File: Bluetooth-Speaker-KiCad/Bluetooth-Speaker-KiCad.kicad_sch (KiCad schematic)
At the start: 34 parts, among them J1 USB4105-GF-A, J2 Screw_Terminal_01x02, J3 Screw_Terminal_01x02, Q1 Q_PMOS_DSG, SW1 SW_Push, SW2 SW_Push, U1 TPD4E02B04DQA, U2 MAX1811, U3 RT6150B-33GQW, U4 MAX98357A, U5 ESP32-C3-WROOM-02

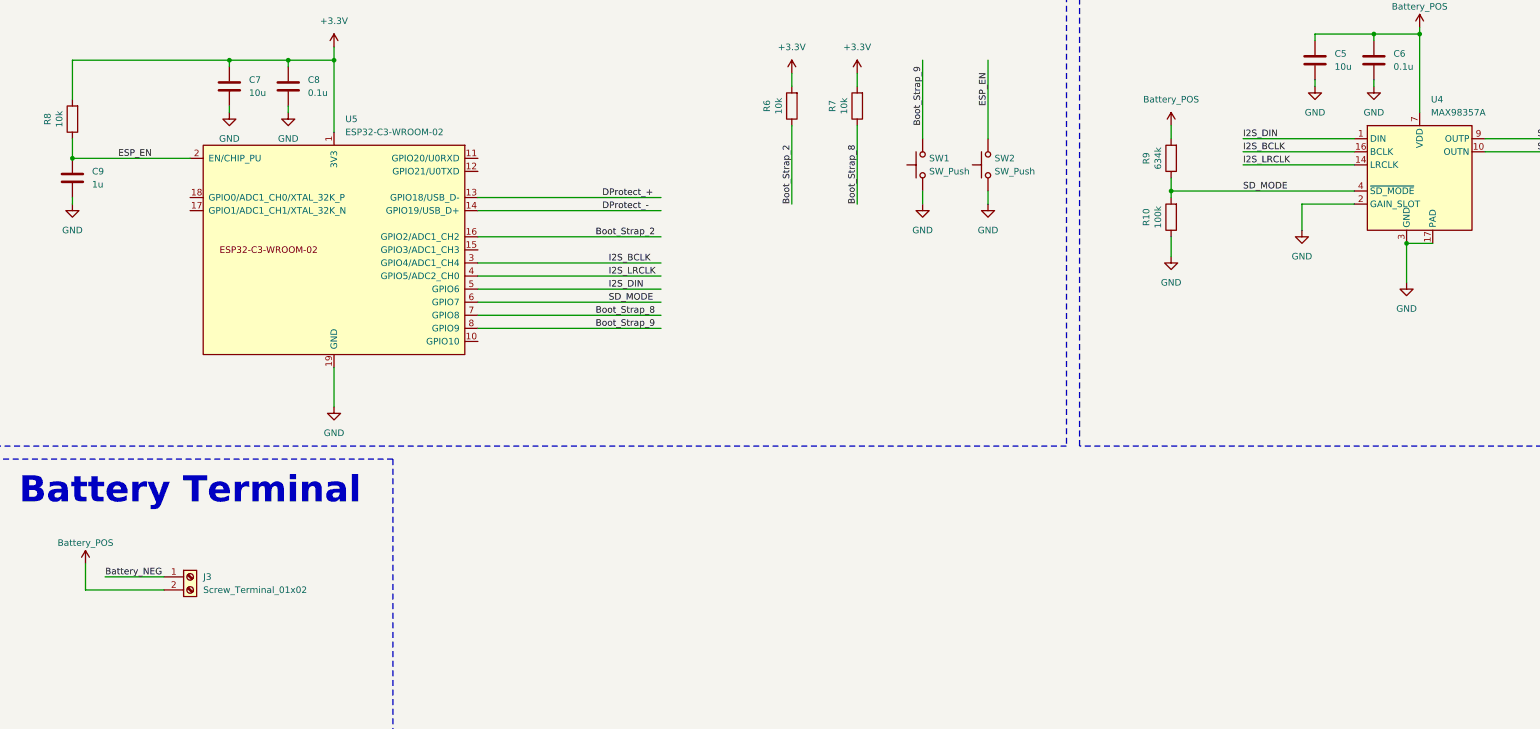
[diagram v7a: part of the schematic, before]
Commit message: Updated layout
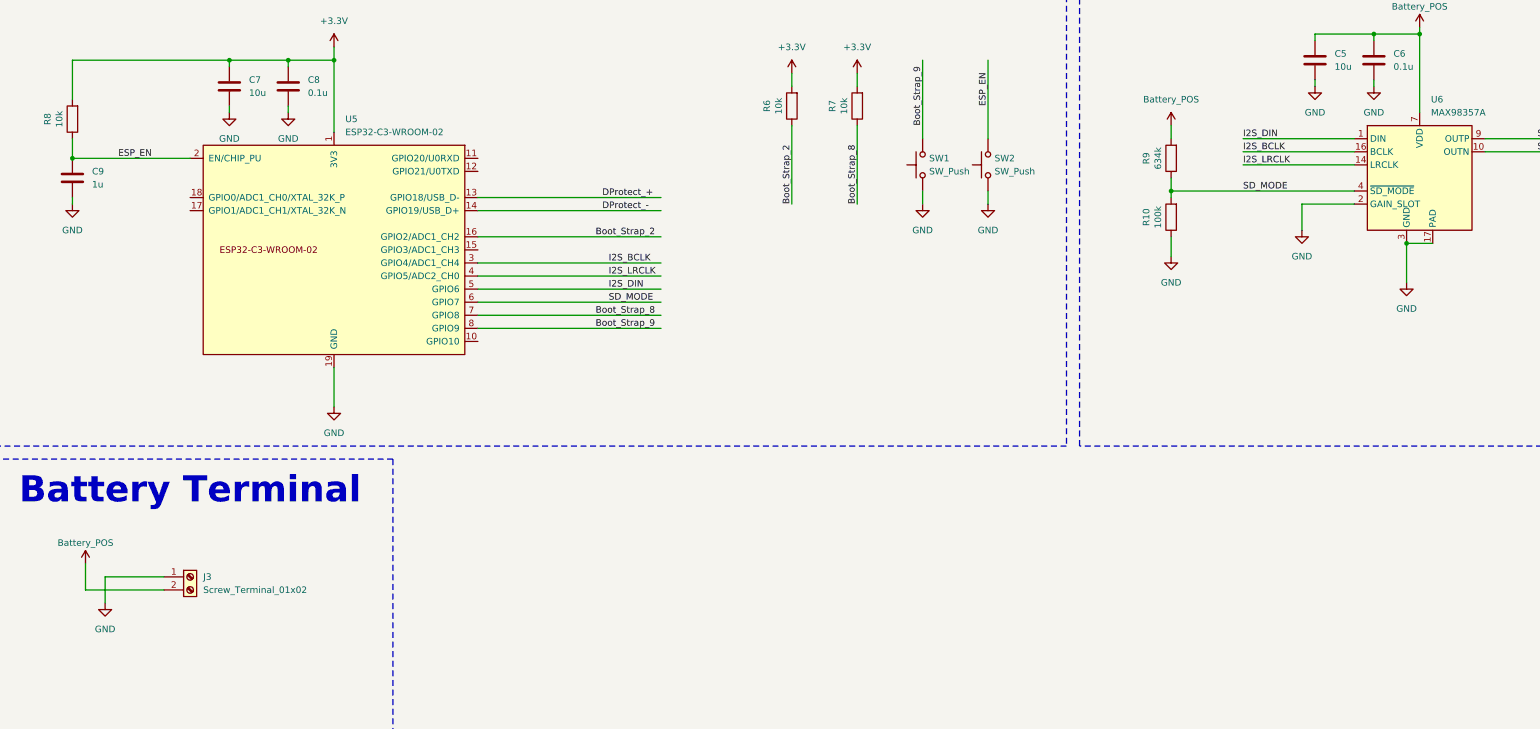
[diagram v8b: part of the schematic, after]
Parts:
- removed U4: MAX98357A, Package_DFN_QFN:TQFN-16-1EP_3x3mm_P0.5mm_EP1.23x1.23mm, symbol Audio:MAX98357A
- added U6: MAX98357A, Package_DFN_QFN:TQFN-16-1EP_3x3mm_P0.5mm_EP1.23x1.23mm_ThermalVias, symbol Audio:MAX98357A
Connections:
- net Battery_NEG is gone; now on net GND: J3.1 (Pin_1)
- net Battery_POS: now also U6.7 (VDD), U6.8 (VDD)
- net GND: now also U6.11 (GND), U6.15 (GND), U6.17 (PAD), U6.2 (GAIN_SLOT), U6.3 (GND)
- net I2S_BCLK: now also U6.16 (BCLK)
- net I2S_DIN: now also U6.1 (DIN)
- net I2S_LRCLK: now also U6.14 (LRCLK)
- net SD_MODE: now also U6.4 (~{SD_MODE})
- net Speaker_NEG: now also U6.10 (OUTN)
- net Speaker_POS: now also U6.9 (OUTP)
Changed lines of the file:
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@@
 	)
 	(junction
-		(at 298.45 177.8)
-		(diameter 0)
-		(color 0 0 0 0)
-	)
-	(junction
 		(at 186.69 63.5)
 		(diameter 0)
@@
 	)
 	(junction
+		(at 298.45 177.8)
+		(diameter 0)
+		(color 0 0 0 0)
+	)
+	(junction
 		(at 237.49 60.96)
 		(diameter 0)
@@
 	(wire
 		(pts
+			(xy 45.72 242.57) (xy 45.72 247.65)
+		)
+		(stroke
+			(width 0)
+			(type default)
+		)
+	)
+	(wire
+		(pts
 			(xy 252.73 167.64) (xy 252.73 168.91)
 		)
@@
 		)
 	)
-	(label "Battery_NEG"
-		(at 45.72 242.57 0)
-		(fields_autoplaced yes)
-		(effects
-			(font
-				(size 1.27 1.27)
-			)
-			(justify left bottom)
-		)
-	)
 	(symbol
 		(lib_id "power:+3.3V")
@@
 	)
 	(symbol
+		(lib_id "Audio:MAX98357A")
+		(at 300.99 165.1 0)
+		(unit 1)
+		(exclude_from_sim no)
+		(in_bom yes)
+		(on_board yes)
+		(dnp no)
+		(fields_autoplaced yes)
+		(property "Reference" "U6"
+			(at 303.1841 149.86 0)
+			(effects
+				(font
+					(size 1.27 1.27)
+				)
+				(justify left)
+			)
+		)
+		(property "Value" "MAX98357A"
+			(at 303.1841 152.4 0)
+			(effects
+				(font
+					(size 1.27 1.27)
+				)
+				(justify left)
+			)
+		)
+		(property "Footprint" "Package_DFN_QFN:TQFN-16-1EP_3x3mm_P0.5mm_EP1.23x1.23mm_ThermalVias"
+			(at 299.72 167.64 0)
+			(effects
+				(font
+					(size 1.27 1.27)
+				)
+				(hide yes)
+			)
+		)
+		(property "Datasheet" "https://www.analog.com/media/en/technical-documentation/data-sheets/MAX98357A-MAX98357B.pdf"
+			(at 300.99 167.64 0)
+			(effects
+				(font
+					(size 1.27 1.27)
+				)
+				(hide yes)
+			)
+		)
+		(property "Description" "Mono DAC with amplifier, I2S, PCM, TDM, 32-bit, 96khz, 3.2W, TQFP-16"
+			(at 300.99 165.1 0)
+			(effects
+				(font
+					(size 1.27 1.27)
+				)
+				(hide yes)
+			)
+		)
+		(pin "3"
+		)
+		(pin "4"
+		)
+		(pin "6"
+		)
+		(pin "5"
+		)
+		(pin "10"
+		)
+		(pin "17"
+		)
+		(pin "8"
+		)
+		(pin "13"
+		)
+		(pin "12"
+		)
+		(pin "1"
+		)
+		(pin "16"
+		)
+		(pin "15"
+		)
+		(pin "14"
+		)
+		(pin "2"
+		)
+		(pin "11"
+		)
+		(pin "7"
+		)
+		(pin "9"
+		)
+		(instances
+			(project ""
+				(path "/d4a3b0fc-2821-415b-ab7a-919b4d2a2ab9"
+					(reference "U6")
+					(unit 1)
+				)
+			)
+		)
+	)
+	(symbol
 		(lib_id "power:GND")
 		(at 278.13 175.26 0)
@@
 	)
 	(symbol
+		(lib_id "power:GND")
+		(at 45.72 247.65 0)
+		(unit 1)
+		(exclude_from_sim no)
+		(in_bom yes)
+		(on_board yes)
+		(dnp no)
+		(fields_autoplaced yes)
+		(property "Reference" "#PWR032"
+			(at 45.72 254 0)
+			(effects
+				(font
+					(size 1.27 1.27)
+				)
+				(hide yes)
+			)
+		)
+		(property "Value" "GND"
+			(at 45.72 252.73 0)
+			(effects
+				(font
+					(size 1.27 1.27)
+				)
+			)
+		)
+		(property "Footprint" ""
+			(at 45.72 247.65 0)
+			(effects
+				(font
+					(size 1.27 1.27)
+				)
+				(hide yes)
+			)
+		)
+		(property "Datasheet" ""
+			(at 45.72 247.65 0)
+			(effects
+				(font
+					(size 1.27 1.27)
+				)
+				(hide yes)
+			)
+		)
+		(property "Description" "Power symbol creates a global label with name \"GND\" , ground"
+			(at 45.72 247.65 0)
+			(effects
+				(font
+					(size 1.27 1.27)
+				)
+				(hide yes)
+			)
+		)
+		(pin "1"
+		)
+		(instances
+			(project "Bluetooth-Speaker-KiCad"
+				(path "/d4a3b0fc-2821-415b-ab7a-919b4d2a2ab9"
+					(reference "#PWR032")
+					(unit 1)
+				)
+			)
+		)
+	)
+	(symbol
 		(lib_id "Device:R")
 		(at 191.77 151.13 180)
@@
 					(unit 1)
 				)
-			)
-		)
-	)
-	(symbol
-		(lib_id "Audio:MAX98357A")
-		(at 300.99 165.1 0)
-		(unit 1)
-		(exclude_from_sim no)
-		(in_bom yes)
-		(on_board yes)
-		(dnp no)
-		(fields_autoplaced yes)
-		(property "Reference" "U4"
-			(at 303.1841 149.86 0)
-			(effects
-				(font
-					(size 1.27 1.27)
-				)
-				(justify left)
-			)
-		)
-		(property "Value" "MAX98357A"
-			(at 303.1841 152.4 0)
-			(effects
-				(font
-					(size 1.27 1.27)
-				)
-				(justify left)
-			)
-		)
-		(property "Footprint" "Package_DFN_QFN:TQFN-16-1EP_3x3mm_P0.5mm_EP1.23x1.23mm"
-			(at 299.72 167.64 0)
-			(effects
-				(font
-					(size 1.27 1.27)
-				)
-				(hide yes)
-			)
-		)
-		(property "Datasheet" "https://www.analog.com/media/en/technical-documentation/data-sheets/MAX98357A-MAX98357B.pdf"
-			(at 300.99 167.64 0)
-			(effects
-				(font
-					(size 1.27 1.27)
-				)
-				(hide yes)
-			)
-		)
-		(property "Description" "Mono DAC with amplifier, I2S, PCM, TDM, 32-bit, 96khz, 3.2W, TQFP-16"
-			(at 300.99 165.1 0)
-			(effects
-				(font
-					(size 1.27 1.27)
-				)
-				(hide yes)
-			)
-		)
-		(pin "4"
-		)
-		(pin "12"
-		)
-		(pin "6"
-		)
-		(pin "17"
-		)
-		(pin "2"
-		)
-		(pin "10"
-		)
-		(pin "16"
-		)
-		(pin "13"
-		)
-		(pin "11"
-		)
-		(pin "1"
-		)
-		(pin "14"
-		)
-		(pin "3"
-		)
-		(pin "7"
-		)
-		(pin "8"
-		)
-		(pin "15"
-		)
-		(pin "9"
-		)
-		(pin "5"
-		)
-		(instances
-			(project ""
-				(path "/d4a3b0fc-2821-415b-ab7a-919b4d2a2ab9"
-					(reference "U4")
-					(unit 1)
-				)
